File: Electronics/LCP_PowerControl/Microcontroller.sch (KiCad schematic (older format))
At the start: 22 parts, among them J5 Conn_02x05_Odd_Even, J6 Conn_02x06_Odd_Even, J7 Conn_02x02_Odd_Even, J8 Conn_02x02_Odd_Even, SW1 SW_Push, U3 MSP430FR5989, Y1 32.768kHz

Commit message: Rev 1 Update
Issues #9-#13 fixed
Rev 1 Gerbers & BOM Ready
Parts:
- removed J6: Conn_02x06_Odd_Even, Connector_PinHeader_2.00mm:PinHeader_2x06_P2.00mm_Vertical, symbol Connector_Generic:Conn_02x06_Odd_Even
- removed J7, J8: Conn_02x02_Odd_Even, Connector_PinHeader_2.00mm:PinHeader_2x02_P2.00mm_Vertical, symbol Connector_Generic:Conn_02x02_Odd_Even
- C14, C15: MPN CBR06C909B5GAC -> CBR06C909BAGAC
- C16: MPN GCJ188R72A102KA01D -> CL10B102KB8NNNC
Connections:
- net ESICI0 is gone; now on net ESICH0: U3.44 (P9.4/ESICI0/A1/C12)
- net ESICI1 is gone; now on net ESICH1: U3.45 (P9.5/ESICI1/A13/C13)
- net DEBUG_RX renamed P3.5
- net DEBUG_TX renamed P3.4
- no-connect marks 12 -> 22
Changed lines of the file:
@@
 Text HLabel 3900 4800 0    50   Output ~ 0
 CONSOLE_RX
-Text HLabel 15050 3800 2    50   Output ~ 0
+Text HLabel 12550 4900 2    50   Output ~ 0
 MD_EN
-Text HLabel 15050 3900 2    50   Output ~ 0
+Text HLabel 12550 5000 2    50   Output ~ 0
 MD_PH
-Text HLabel 15050 4100 2    50   Input ~ 0
+Text HLabel 12550 5200 2    50   Input ~ 0
 ~MD_FAULT
-Text HLabel 15050 4200 2    50   UnSpc ~ 0
+Text HLabel 12550 5300 2    50   UnSpc ~ 0
 MD_IPROPI
-Text HLabel 15050 4300 2    50   Output ~ 0
+Text HLabel 12550 5400 2    50   Output ~ 0
 MD_PMODE
-Text HLabel 15050 4000 2    50   Output ~ 0
+Text HLabel 12550 5100 2    50   Output ~ 0
 ~MD_SLEEP
 Text HLabel 3900 5550 0    50   Output ~ 0
@@
 F 2 "Capacitor_SMD:C_0603_1608Metric" H 10450 6250 50  0001 C CNN
 F 3 "~" H 10450 6250 50  0001 C CNN
-F 4 "CBR06C909B5GAC" V 10450 6250 50  0001 C CNN "MPN"
+F 4 "CBR06C909BAGAC" V 10450 6250 50  0001 C CNN "MPN"
 	1    10450 6250
 	0    1    1    0
@@
 F 2 "Capacitor_SMD:C_0603_1608Metric" H 10450 6750 50  0001 C CNN
 F 3 "~" H 10450 6750 50  0001 C CNN
-F 4 "CBR06C909B5GAC" V 10450 6750 50  0001 C CNN "MPN"
+F 4 "CBR06C909BAGAC" V 10450 6750 50  0001 C CNN "MPN"
 	1    10450 6750
 	0    1    1    0
@@
 F 2 "Capacitor_SMD:C_0603_1608Metric" H 12188 3550 50  0001 C CNN
 F 3 "~" H 12150 3700 50  0001 C CNN
-F 4 "GCJ188R72A102KA01D" H 12150 3700 50  0001 C CNN "MPN"
+F 4 "CL10B102KB8NNNC" H 12150 3700 50  0001 C CNN "MPN"
 	1    12150 3700
 	1    0    0    -1
@@
 Wire Wire Line
 	6650 5300 6200 5300
-Text HLabel 3900 4050 0    50   Output ~ 0
-DEBUG_TX
-Wire Wire Line
-	3900 4050 6650 4050
-Text HLabel 3900 4150 0    50   Input ~ 0
-DEBUG_RX
-Wire Wire Line
-	3900 4150 6650 4150
 Text HLabel 3900 4250 0    50   Output ~ 0
 DEBUG_LED_1
@@
 P4.2
 Wire Wire Line
-	14750 3900 15050 3900
-Text GLabel 14750 4000 0    50   BiDi ~ 0
+	12250 5000 12550 5000
+Text GLabel 12250 5100 0    50   BiDi ~ 0
 P4.3
 Wire Wire Line
-	14750 4000 15050 4000
-Text GLabel 14750 4100 0    50   BiDi ~ 0
+	12250 5100 12550 5100
+Text GLabel 12250 5200 0    50   BiDi ~ 0
 P5.0
 Wire Wire Line
-	14750 4100 15050 4100
+	12250 5200 12550 5200
 Text GLabel 6200 5500 0    50   UnSpc ~ 0
 ADC2
 Wire Wire Line
 	6200 5500 6650 5500
-Text GLabel 14750 3800 0    50   Input ~ 0
+Text GLabel 12250 4900 0    50   Input ~ 0
 PWM_TB0.3
-Text GLabel 14750 4200 0    50   UnSpc ~ 0
+Text GLabel 12250 5300 0    50   UnSpc ~ 0
 ADC2
 Wire Wire Line
-	14750 4200 15050 4200
-Text GLabel 14750 4300 0    50   BiDi ~ 0
+	12250 5300 12550 5300
+Text GLabel 12250 5400 0    50   BiDi ~ 0
 P5.1
 Wire Wire Line
-	14750 4300 15050 4300
-Text GLabel 12250 7950 0    50   Input ~ 0
+	12250 5400 12550 5400
+Text GLabel 12250 6450 0    50   Input ~ 0
 ESICH0
-Text GLabel 12250 8050 0    50   Input ~ 0
+Text GLabel 12250 6550 0    50   Input ~ 0
 ESICH1
-Text GLabel 12250 8150 0    50   Input ~ 0
+Text GLabel 12250 6650 0    50   Input ~ 0
 ESICH2
-Text GLabel 12250 8250 0    50   Input ~ 0
+Text GLabel 12250 6750 0    50   Input ~ 0
 ESICH3
-Text GLabel 13300 7950 2    50   Input ~ 0
+Text GLabel 12950 6550 2    50   Input ~ 0
+ESICI1
+Text GLabel 12950 6650 2    50   Input ~ 0
+ESICI2
+Text GLabel 12950 6750 2    50   Input ~ 0
+ESICI3
+Text GLabel 12250 6850 0    50   Input ~ 0
+ESICI
+Text GLabel 12950 6850 2    50   Input ~ 0
+ESICOM
+Text HLabel 12550 5750 2    50   Input ~ 0
+ENCODER_CH_A
+Text HLabel 12550 5850 2    50   Input ~ 0
+ENCODER_CH_B
+Text GLabel 12250 5750 0    50   Input ~ 0
 ESICI0
-Text GLabel 13300 8050 2    50   Input ~ 0
+Text GLabel 12250 5850 0    50   Input ~ 0
 ESICI1
-Text GLabel 13300 8150 2    50   Input ~ 0
-ESICI2
-Text GLabel 13300 8250 2    50   Input ~ 0
-ESICI3
-$Comp
-L Connector_Generic:Conn_02x06_Odd_Even J6
-U 1 1 5F0F003E
-P 12700 8050
-F 0 "J6" H 12750 8350 50  0000 C CNN
-F 1 "Conn_02x06_Odd_Even" H 12750 7650 50  0000 C CNN
-F 2 "Connector_PinHeader_2.00mm:PinHeader_2x06_P2.00mm_Vertical" H 12700 8050 50  0001 C CNN
-F 3 "~" H 12700 8050 50  0001 C CNN
-F 4 "2842126-6" H 12700 8050 50  0001 C CNN "MPN"
-	1    12700 8050
-	1    0    0    -1
-$EndComp
-Text GLabel 12250 8350 0    50   Input ~ 0
-ESICI
-Text GLabel 13300 8350 2    50   Input ~ 0
-ESICOM
-Wire Wire Line
-	13300 8350 13000 8350
-Wire Wire Line
-	13000 8250 13300 8250
-Wire Wire Line
-	13300 8150 13000 8150
-Wire Wire Line
-	13000 8050 13300 8050
-Wire Wire Line
-	13300 7950 13000 7950
-Wire Wire Line
-	12500 7950 12250 7950
-Wire Wire Line
-	12250 8050 12500 8050
-Wire Wire Line
-	12500 8150 12250 8150
-Wire Wire Line
-	12250 8250 12500 8250
-Wire Wire Line
-	12250 8350 12500 8350
-$Comp
-L power:GND #PWR031
-U 1 1 5F139610
-P 13450 7650
-F 0 "#PWR031" H 13450 7400 50  0001 C CNN
-F 1 "GND" H 13455 7477 50  0000 C CNN
-F 2 "" H 13450 7650 50  0001 C CNN
-F 3 "" H 13450 7650 50  0001 C CNN
-	1    13450 7650
-	1    0    0    -1
-$EndComp
-Wire Wire Line
-	13000 7850 13100 7850
-Wire Wire Line
-	13100 7850 13100 7550
-Wire Wire Line
-	13100 7550 13450 7550
-Wire Wire Line
-	13450 7550 13450 7650
-$Comp
-L power:+3V3 #PWR030
-U 1 1 5F141006
-P 12250 7700
-F 0 "#PWR030" H 12250 7550 50  0001 C CNN
-F 1 "+3V3" H 12265 7873 50  0000 C CNN
-F 2 "" H 12250 7700 50  0001 C CNN
-F 3 "" H 12250 7700 50  0001 C CNN
-	1    12250 7700
-	1    0    0    -1
-$EndComp
-Wire Wire Line
-	12250 7700 12250 7850
-Wire Wire Line
-	12250 7850 12500 7850
-Text HLabel 15000 6400 2    50   Input ~ 0
-ENCODER_CH_A
-Text HLabel 15000 6500 2    50   Input ~ 0
-ENCODER_CH_B
-Text GLabel 13850 6150 0    50   Input ~ 0
-ESICI0
-Text GLabel 13850 6650 0    50   Input ~ 0
-ESICI1
-$Comp
-L Connector_Generic:Conn_02x02_Odd_Even J7
-U 1 1 5F17BAA5
-P 14200 6150
-F 0 "J7" H 14250 6250 50  0000 C CNN
-F 1 "Conn_02x02_Odd_Even" H 14250 5950 50  0000 C CNN
-F 2 "Connector_PinHeader_2.00mm:PinHeader_2x02_P2.00mm_Vertical" H 14200 6150 50  0001 C CNN
-F 3 "~" H 14200 6150 50  0001 C CNN
-F 4 "5176264-1" H 14200 6150 50  0001 C CNN "MPN"
-	1    14200 6150
-	1    0    0    -1
-$EndComp
-$Comp
-L Connector_Generic:Conn_02x02_Odd_Even J8
-U 1 1 5F17C61B
-P 14200 6650
-F 0 "J8" H 14250 6750 50  0000 C CNN
-F 1 "Conn_02x02_Odd_Even" H 14250 6450 50  0000 C CNN
-F 2 "Connector_PinHeader_2.00mm:PinHeader_2x02_P2.00mm_Vertical" H 14200 6650 50  0001 C CNN
-F 3 "~" H 14200 6650 50  0001 C CNN
-F 4 "5176264-1" H 14200 6650 50  0001 C CNN "MPN"
-	1    14200 6650
-	1    0    0    -1
-$EndComp
-Wire Wire Line
-	14500 6150 14600 6150
-Wire Wire Line
-	14600 6150 14600 6200
-Wire Wire Line
-	14600 6250 14500 6250
-Wire Wire Line
-	14500 6650 14600 6650
-Wire Wire Line
-	14600 6650 14600 6700
-Wire Wire Line
-	14600 6750 14500 6750
-Wire Wire Line
-	14600 6700 14700 6700
-Wire Wire Line
-	14700 6700 14700 6500
-Wire Wire Line
-	14700 6500 15000 6500
-Connection ~ 14600 6700
-Wire Wire Line
-	14600 6700 14600 6750
-Wire Wire Line
-	15000 6400 14700 6400
-Wire Wire Line
-	14700 6400 14700 6200
-Wire Wire Line
-	14700 6200 14600 6200
-Connection ~ 14600 6200
-Wire Wire Line
-	14600 6200 14600 6250
-Wire Wire Line
-	14000 6650 13850 6650
-Wire Wire Line
-	14000 6150 13850 6150
-Text GLabel 13850 6250 0    50   Input ~ 0
-P1.1
-Wire Wire Line
-	13850 6250 14000 6250
+Wire Wire Line
+	12250 5850 12550 5850
+Wire Wire Line
+	12550 5750 12250 5750
 Text GLabel 4350 5550 2    50   Input ~ 0
 P2.5
@@
 Wire Wire Line
 	10150 3950 9900 3950
-Text GLabel 14750 3900 0    50   BiDi ~ 0
+Text GLabel 12250 5000 0    50   BiDi ~ 0
 P2.6
 Text GLabel 6750 9050 0    50   BiDi ~ 0
 P2.7
-Text GLabel 13850 6750 0    50   BiDi ~ 0
+Text GLabel 6750 9150 0    50   BiDi ~ 0
 P1.3
 Text GLabel 6450 4600 0    50   BiDi ~ 0
@@
 Connection ~ 4250 3150
 Wire Wire Line
-	13850 6750 14000 6750
-Wire Wire Line
-	14750 3800 15050 3800
+	12250 4900 12550 4900
 Text HLabel 3900 4700 0    50   Input ~ 0
 CONSOLE_PWR
@@
 	0    1    1    0
 $EndComp
+Text GLabel 7250 8650 0    50   BiDi ~ 0
+P3.3
+Text GLabel 7250 9150 0    50   Input ~ 0
+P1.1
+NoConn ~ 6750 9150
+NoConn ~ 7250 9150
+Text GLabel 12950 6450 2    50   Input ~ 0
+ESICI0
+Wire Wire Line
+	12250 6450 12950 6450
+Wire Wire Line
+	12950 6550 12250 6550
+Text GLabel 6750 9250 0    50   BiDi ~ 0
+P3.4
+Text GLabel 7250 9250 0    50   BiDi ~ 0
+P3.5
+NoConn ~ 6750 9250
+NoConn ~ 7250 9250
+NoConn ~ 12250 6650
+NoConn ~ 12250 6750
+NoConn ~ 12250 6850
+NoConn ~ 12950 6850
+NoConn ~ 12950 6750
+NoConn ~ 12950 6650
+Text GLabel 6500 4050 0    50   BiDi ~ 0
+P3.4
+Wire Wire Line
+	6500 4050 6650 4050
+Text GLabel 6500 4150 0    50   BiDi ~ 0
+P3.5
+Wire Wire Line
+	6650 4150 6500 4150
 $EndSCHEMATC

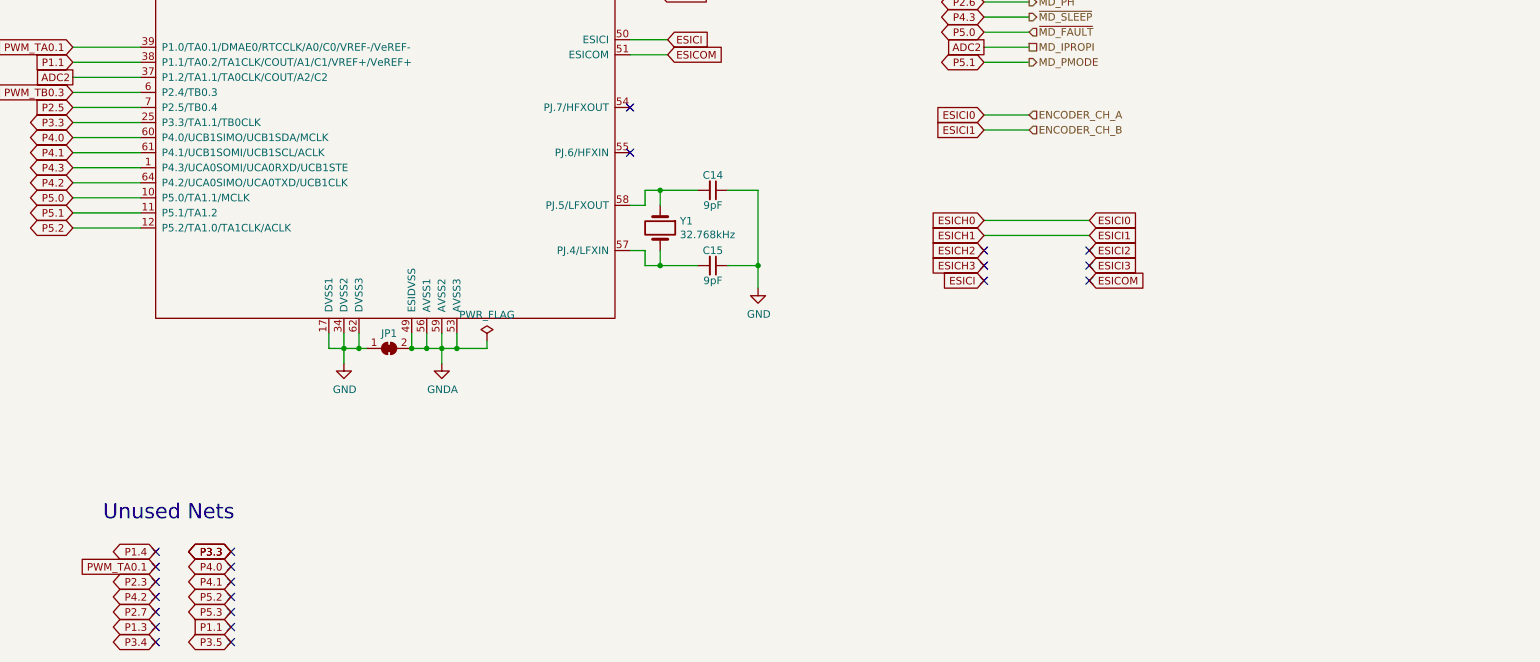
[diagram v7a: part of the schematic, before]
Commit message: Adding selection for GPIO encoder read.
Adding P1.3/4 for encoder A/B read
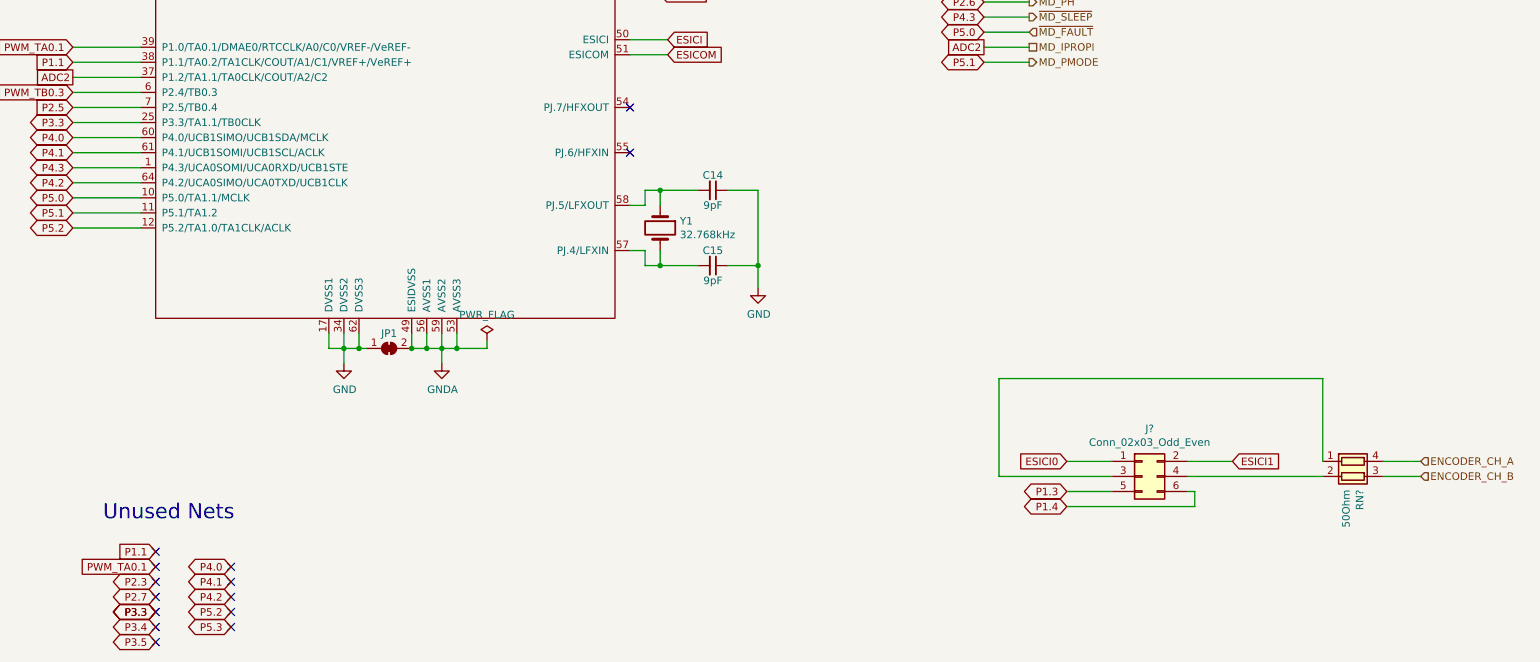
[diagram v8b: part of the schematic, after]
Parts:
- added J?: Conn_02x03_Odd_Even, Connector_PinHeader_2.54mm:PinHeader_2x03_P2.54mm_Vertical, symbol Connector_Generic:Conn_02x03_Odd_Even
- added RN?: 50Ohm, Resistor_SMD:R_Array_Concave_2x0603, symbol Device:R_Pack02
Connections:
- net ESICH0: no longer U3.44 (P9.4/ESICI0/A1/C12)
- net ESICH1: no longer U3.45 (P9.5/ESICI1/A13/C13)
- net P1.3: now also J?.5 (Pin_5)
- net P1.4: now also J?.6 (Pin_6)
- new net: J?.3 (Pin_3), RN?.1 (R1.1)
- new net: J?.4 (Pin_4), RN?.2 (R2.1)
- new net ENCODER_CH_A: RN?.4 (R1.2)
- new net ENCODER_CH_B: RN?.3 (R2.2)
- new net ESICI0: J?.1 (Pin_1), U3.44 (P9.4/ESICI0/A1/C12)
- new net ESICI1: J?.2 (Pin_2), U3.45 (P9.5/ESICI1/A13/C13)
- no-connect marks 22 -> 14
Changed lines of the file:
@@
 Wire Wire Line
 	6200 6300 6650 6300
-Text GLabel 6750 8950 0    50   BiDi ~ 0
+Text GLabel 7250 8950 0    50   BiDi ~ 0
 P4.2
 Wire Wire Line
@@
 Wire Wire Line
 	12250 5400 12550 5400
-Text GLabel 12250 6450 0    50   Input ~ 0
-ESICH0
-Text GLabel 12250 6550 0    50   Input ~ 0
-ESICH1
-Text GLabel 12250 6650 0    50   Input ~ 0
-ESICH2
-Text GLabel 12250 6750 0    50   Input ~ 0
-ESICH3
-Text GLabel 12950 6550 2    50   Input ~ 0
+Text HLabel 15150 8050 2    50   Input ~ 0
+ENCODER_CH_A
+Text HLabel 15150 8150 2    50   Input ~ 0
+ENCODER_CH_B
+Text GLabel 12800 8050 0    50   Input ~ 0
+ESICI0
+Text GLabel 13900 8050 2    50   Input ~ 0
 ESICI1
-Text GLabel 12950 6650 2    50   Input ~ 0
-ESICI2
-Text GLabel 12950 6750 2    50   Input ~ 0
-ESICI3
-Text GLabel 12250 6850 0    50   Input ~ 0
-ESICI
-Text GLabel 12950 6850 2    50   Input ~ 0
-ESICOM
-Text HLabel 12550 5750 2    50   Input ~ 0
-ENCODER_CH_A
-Text HLabel 12550 5850 2    50   Input ~ 0
-ENCODER_CH_B
-Text GLabel 12250 5750 0    50   Input ~ 0
-ESICI0
-Text GLabel 12250 5850 0    50   Input ~ 0
-ESICI1
-Wire Wire Line
-	12250 5850 12550 5850
-Wire Wire Line
-	12550 5750 12250 5750
 Text GLabel 4350 5550 2    50   Input ~ 0
 P2.5
@@
 Text GLabel 7250 8850 0    50   BiDi ~ 0
 P4.1
-Text GLabel 7250 8950 0    50   BiDi ~ 0
+Text GLabel 7250 9050 0    50   BiDi ~ 0
 P5.2
 Text GLabel 6500 2950 0    50   BiDi ~ 0
@@
 Wire Wire Line
 	6500 3500 6650 3500
-Text GLabel 7250 9050 0    50   BiDi ~ 0
+Text GLabel 7250 9150 0    50   BiDi ~ 0
 P5.3
-Text GLabel 6750 8650 0    50   BiDi ~ 0
+Text GLabel 12800 8350 0    50   BiDi ~ 0
 P1.4
 Text GLabel 10150 3950 2    50   BiDi ~ 0
@@
 Text GLabel 12250 5000 0    50   BiDi ~ 0
 P2.6
-Text GLabel 6750 9050 0    50   BiDi ~ 0
+Text GLabel 6750 8950 0    50   BiDi ~ 0
 P2.7
-Text GLabel 6750 9150 0    50   BiDi ~ 0
+Text GLabel 12800 8250 0    50   BiDi ~ 0
 P1.3
 Text GLabel 6450 4600 0    50   BiDi ~ 0
@@
 Wire Wire Line
 	6650 5800 6200 5800
-Text GLabel 7250 8650 0    50   BiDi ~ 0
+Text GLabel 6750 9050 0    50   BiDi ~ 0
 P3.3
-NoConn ~ 6750 8650
 NoConn ~ 6750 8850
+NoConn ~ 7250 8950
 NoConn ~ 6750 8950
-NoConn ~ 6750 9050
+NoConn ~ 7250 9150
 NoConn ~ 7250 9050
-NoConn ~ 7250 8950
 NoConn ~ 7250 8850
 NoConn ~ 7250 8750
-NoConn ~ 7250 8650
+NoConn ~ 6750 9050
 Text Notes 6400 8450 0    100  ~ 0
 Unused Nets
@@
 	0    1    1    0
 $EndComp
-Text GLabel 7250 8650 0    50   BiDi ~ 0
+Text GLabel 6750 9050 0    50   BiDi ~ 0
 P3.3
-Text GLabel 7250 9150 0    50   Input ~ 0
+Text GLabel 6750 8650 0    50   Input ~ 0
 P1.1
+NoConn ~ 6750 8650
+Text GLabel 6750 9150 0    50   BiDi ~ 0
+P3.4
+Text GLabel 6750 9250 0    50   BiDi ~ 0
+P3.5
 NoConn ~ 6750 9150
-NoConn ~ 7250 9150
-Text GLabel 12950 6450 2    50   Input ~ 0
-ESICI0
-Wire Wire Line
-	12250 6450 12950 6450
-Wire Wire Line
-	12950 6550 12250 6550
-Text GLabel 6750 9250 0    50   BiDi ~ 0
-P3.4
-Text GLabel 7250 9250 0    50   BiDi ~ 0
-P3.5
 NoConn ~ 6750 9250
-NoConn ~ 7250 9250
-NoConn ~ 12250 6650
-NoConn ~ 12250 6750
-NoConn ~ 12250 6850
-NoConn ~ 12950 6850
-NoConn ~ 12950 6750
-NoConn ~ 12950 6650
 Text GLabel 6500 4050 0    50   BiDi ~ 0
 P3.4
@@
 Wire Wire Line
 	6650 4150 6500 4150
+$Comp
+L Connector_Generic:Conn_02x03_Odd_Even J?
+U 1 1 60479EE2
+P 13300 8150
+F 0 "J?" H 13350 8467 50  0000 C CNN
+F 1 "Conn_02x03_Odd_Even" H 13350 8376 50  0000 C CNN
+F 2 "Connector_PinHeader_2.54mm:PinHeader_2x03_P2.54mm_Vertical" H 13300 8150 50  0001 C CNN
+F 3 "~" H 13300 8150 50  0001 C CNN
+	1    13300 8150
+	1    0    0    -1
+$EndComp
+Wire Wire Line
+	12800 8050 13100 8050
+Wire Wire Line
+	13900 8050 13600 8050
+$Comp
+L Device:R_Pack02 RN?
+U 1 1 604C7193
+P 14700 8150
+F 0 "RN?" H 14788 8196 50  0000 L CNN
+F 1 "50Ohm" H 14788 8105 50  0000 L CNN
+F 2 "Resistor_SMD:R_Array_Concave_2x0603" V 14875 8150 50  0001 C CNN
+F 3 "~" H 14700 8150 50  0001 C CNN
+F 4 "EXB-V4V510JV" H 14700 8150 50  0001 C CNN "MPN"
+	1    14700 8150
+	0    1    1    0
+$EndComp
+Wire Wire Line
+	13100 8250 12800 8250
+Wire Wire Line
+	12800 8350 13650 8350
+Wire Wire Line
+	13650 8350 13650 8250
+Wire Wire Line
+	13650 8250 13600 8250
+Wire Wire Line
+	14500 8150 13600 8150
+Wire Wire Line
+	14500 8050 14500 7500
+Wire Wire Line
+	14500 7500 12350 7500
+Wire Wire Line
+	12350 7500 12350 8150
+Wire Wire Line
+	12350 8150 13100 8150
+Wire Wire Line
+	15150 8150 14900 8150
+Wire Wire Line
+	15150 8050 14900 8050
 $EndSCHEMATC
